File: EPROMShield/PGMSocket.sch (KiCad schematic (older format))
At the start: 22 parts

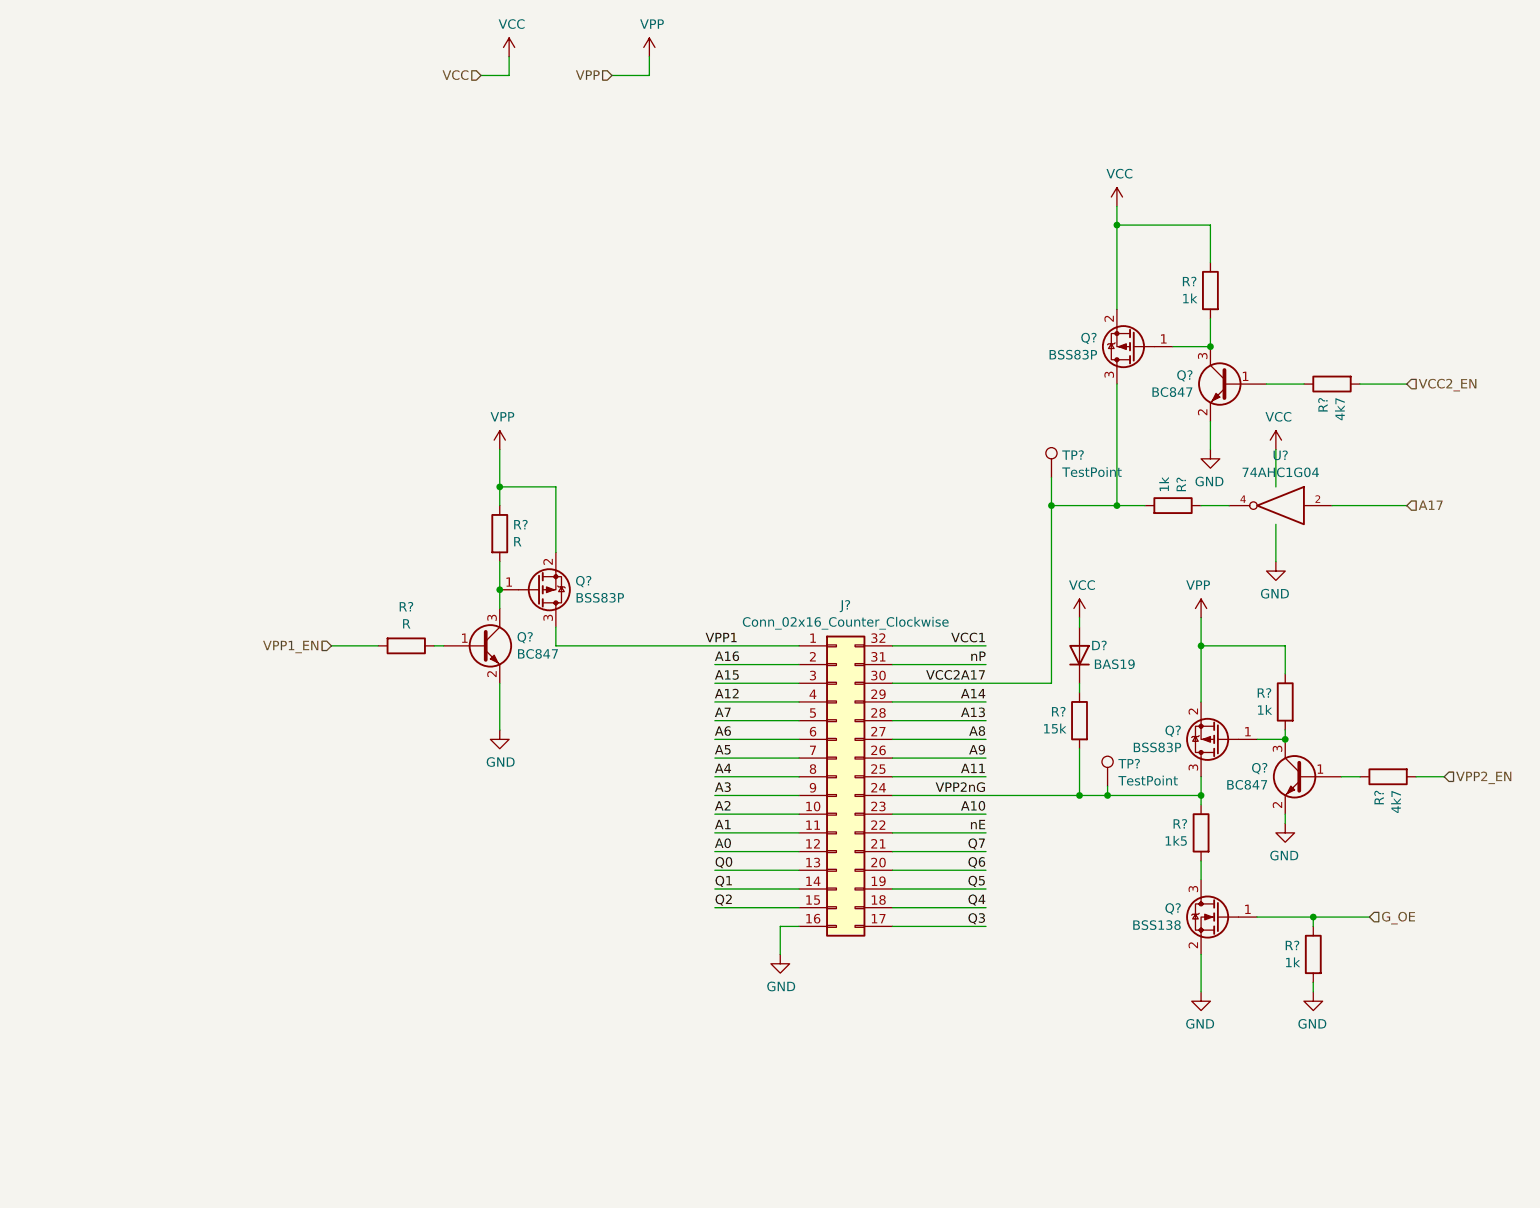
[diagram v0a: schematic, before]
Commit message: Finished schematic added caluclation for boost converter
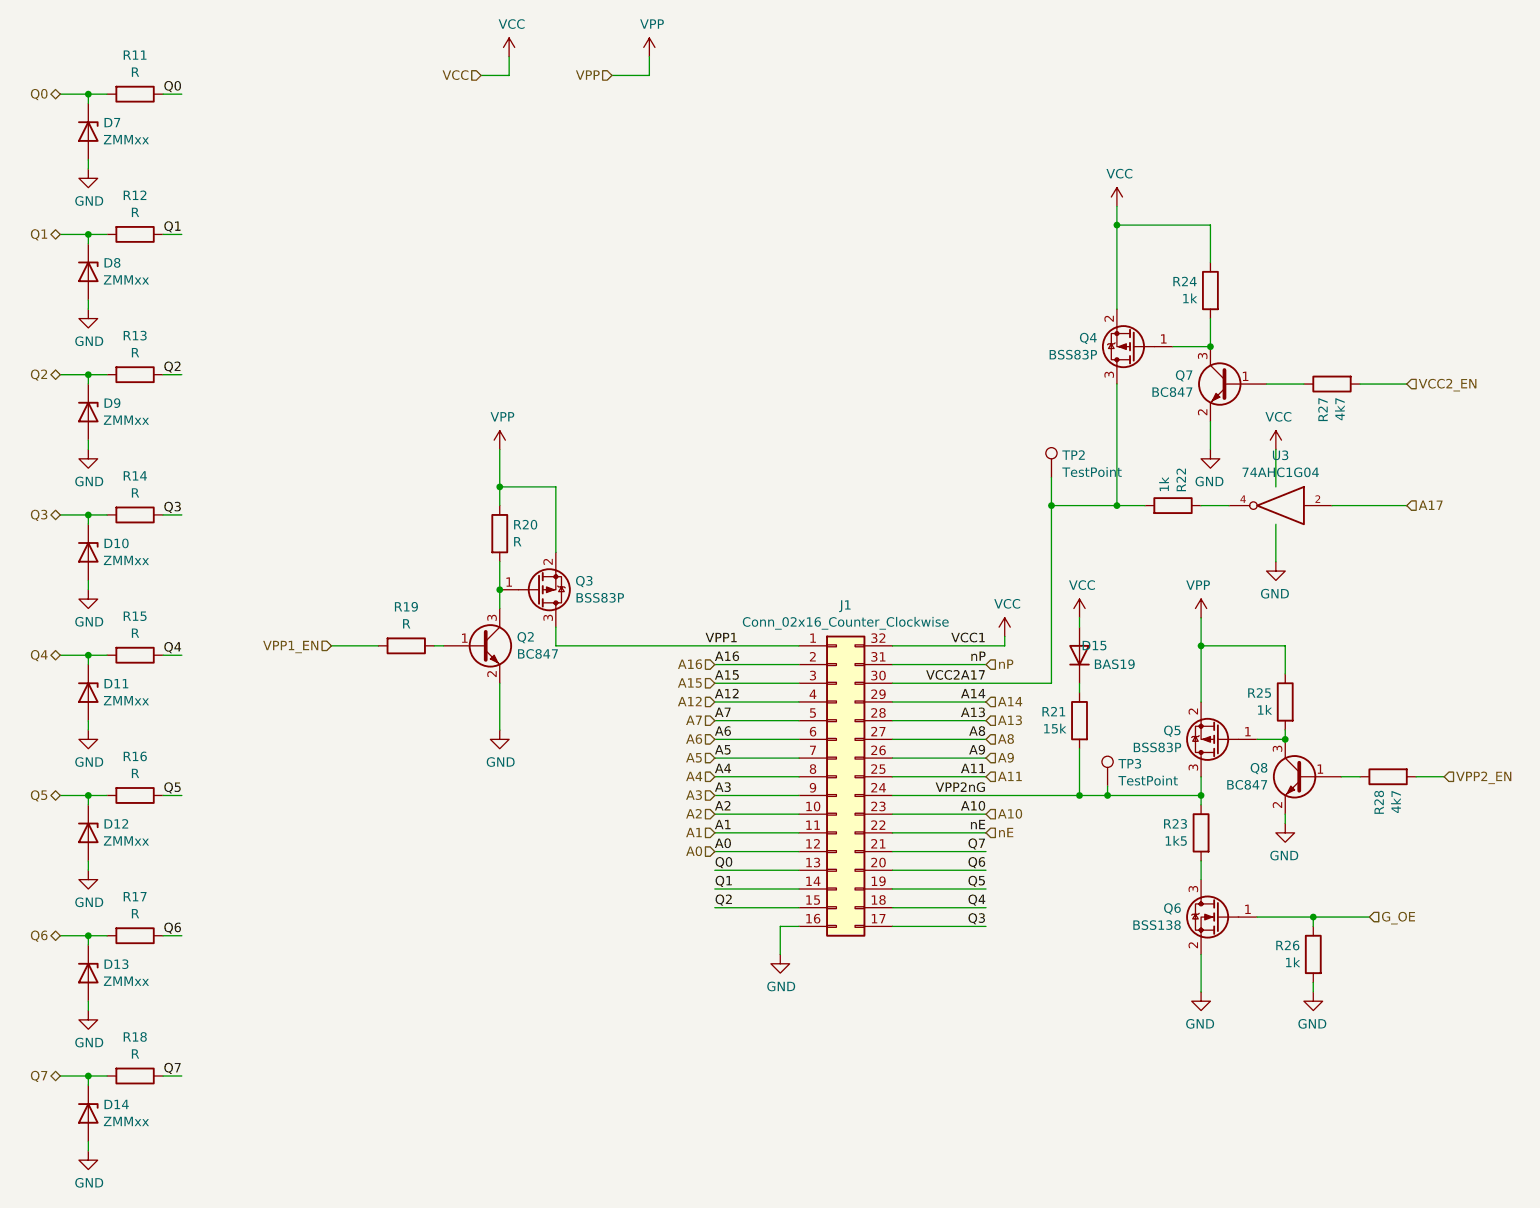
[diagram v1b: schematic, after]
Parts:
- added D10, D11, D12, D13, D14, D7, D8, D9: ZMMxx, Diode_SMD:D_MiniMELF, symbol Diode:ZMMxx
- added R11, R12, R13, R14, R15, R16, R17, R18: R, symbol Device:R
- gave numbers to parts that had none: 22
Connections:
- net VCC1 is gone; now on net VCC: J1.32 (Pin_32)
- net GND: now also D10.2 (A), D11.2 (A), D12.2 (A), D13.2 (A), D14.2 (A), D7.2 (A), D8.2 (A), D9.2 (A)
- net Q0: now also D7.1 (K), R11.1, R11.2
- net Q1: now also D8.1 (K), R12.1, R12.2
- net Q2: now also D9.1 (K), R13.1, R13.2
- net Q3: now also D10.1 (K), R14.1, R14.2
- net Q4: now also D11.1 (K), R15.1, R15.2
- net Q5: now also D12.1 (K), R16.1, R16.2
- net Q6: now also D13.1 (K), R17.1, R17.2
- net Q7: now also D14.1 (K), R18.1, R18.2

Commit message: Footprints associated
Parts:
- removed U3: 74AHC1G04, symbol 74xGxx:74AHC1G04
- added U3: 74AHC1GU04, Package_TO_SOT_SMD:SOT-353_SC-70-5_Handsoldering, symbol 74xGxx:74AHC1GU04
- J1: footprint (none) -> Socket:DIP_Socket-32_W11.9_W12.7_W15.24_W17.78_W18.5_3M_232-1285-00-0602J
- R11, R12, R13, R14, R15, R16, R17, R18: value R -> 1k2; footprint (none) -> Resistor_SMD:R_0805_2012Metric_Pad1.20x1.40mm_HandSolder
- R19: value R -> 4k7; footprint (none) -> Resistor_SMD:R_0805_2012Metric_Pad1.20x1.40mm_HandSolder
- R20: value R -> 10k; footprint (none) -> Resistor_SMD:R_0805_2012Metric_Pad1.20x1.40mm_HandSolder
- R21, R22, R23, R26, R27, R28: footprint (none) -> Resistor_SMD:R_0805_2012Metric_Pad1.20x1.40mm_HandSolder
- R24, R25: value 1k -> 10k; footprint (none) -> Resistor_SMD:R_0805_2012Metric_Pad1.20x1.40mm_HandSolder
- TP2, TP3: footprint (none) -> TestPoint:TestPoint_Pad_D2.0mm
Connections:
- net VCC is gone; now on net GND: D15.1 (A), J1.32 (Pin_32), Q4.2 (S), R24.1
- net A17: now also U3.2
- net GND: now also U3.3 (GND), U3.5 (VCC)
- net at R22.1: now also U3.4
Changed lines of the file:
@@
 F 0 "J1" H 5300 5517 50  0000 C CNN
 F 1 "Conn_02x16_Counter_Clockwise" H 5300 5426 50  0000 C CNN
-F 2 "" H 5250 4600 50  0001 C CNN
+F 2 "Socket:DIP_Socket-32_W11.9_W12.7_W15.24_W17.78_W18.5_3M_232-1285-00-0602J" H 5250 4600 50  0001 C CNN
 F 3 "~" H 5250 4600 50  0001 C CNN
 	1    5250 4600
@@
 P 3450 3300
 F 0 "R20" H 3520 3346 50  0000 L CNN
-F 1 "R" H 3520 3255 50  0000 L CNN
-F 2 "" V 3380 3300 50  0001 C CNN
+F 1 "10k" H 3520 3255 50  0000 L CNN
+F 2 "Resistor_SMD:R_0805_2012Metric_Pad1.20x1.40mm_HandSolder" V 3380 3300 50  0001 C CNN
 F 3 "~" H 3450 3300 50  0001 C CNN
 	1    3450 3300
@@
 AR Path="/6126FB03/616FB69F" Ref="R19"  Part="1"
 F 0 "R19" V 2743 3900 50  0000 C CNN
-F 1 "R" V 2834 3900 50  0000 C CNN
-F 2 "" V 2880 3900 50  0001 C CNN
+F 1 "4k7" V 2834 3900 50  0000 C CNN
+F 2 "Resistor_SMD:R_0805_2012Metric_Pad1.20x1.40mm_HandSolder" V 2880 3900 50  0001 C CNN
 F 3 "~" H 2950 3900 50  0001 C CNN
 	1    2950 3900
@@
 P 7650 4200
 F 0 "R25" H 7720 4246 50  0000 L CNN
-F 1 "1k" H 7720 4155 50  0000 L CNN
-F 2 "" V 7580 4200 50  0001 C CNN
+F 1 "10k" H 7720 4155 50  0000 L CNN
+F 2 "Resistor_SMD:R_0805_2012Metric_Pad1.20x1.40mm_HandSolder" V 7580 4200 50  0001 C CNN
 F 3 "~" H 7650 4200 50  0001 C CNN
 	1    7650 4200
@@
 F 0 "R28" H 8270 4646 50  0000 L CNN
 F 1 "4k7" H 8270 4555 50  0000 L CNN
-F 2 "" V 8130 4600 50  0001 C CNN
+F 2 "Resistor_SMD:R_0805_2012Metric_Pad1.20x1.40mm_HandSolder" V 8130 4600 50  0001 C CNN
 F 3 "~" H 8200 4600 50  0001 C CNN
 	1    8200 4600
@@
 F 0 "R26" H 7870 5596 50  0000 L CNN
 F 1 "1k" H 7870 5505 50  0000 L CNN
-F 2 "" V 7730 5550 50  0001 C CNN
+F 2 "Resistor_SMD:R_0805_2012Metric_Pad1.20x1.40mm_HandSolder" V 7730 5550 50  0001 C CNN
 F 3 "~" H 7800 5550 50  0001 C CNN
 	1    7800 5550
@@
 F 0 "R23" H 7270 4946 50  0000 L CNN
 F 1 "1k5" H 7270 4855 50  0000 L CNN
-F 2 "" V 7130 4900 50  0001 C CNN
+F 2 "Resistor_SMD:R_0805_2012Metric_Pad1.20x1.40mm_HandSolder" V 7130 4900 50  0001 C CNN
 F 3 "~" H 7200 4900 50  0001 C CNN
 	1    7200 4900
@@
 Wire Wire Line
 	7200 5050 7200 5150
-$Comp
-L 74xGxx:74AHC1G04 U3
-U 1 1 616FB717
-P 7600 3150
-F 0 "U3" H 7575 3417 50  0000 C CNN
-F 1 "74AHC1G04" H 7575 3326 50  0000 C CNN
-F 2 "" H 7600 3150 50  0001 C CNN
-F 3 "http://www.ti.com/lit/sg/scyt129e/scyt129e.pdf" H 7600 3150 50  0001 C CNN
-	1    7600 3150
-	-1   0    0    -1
-$EndComp
 $Comp
 L power:VCC #PWR?
@@
 F 0 "R27" H 7970 2546 50  0000 L CNN
 F 1 "4k7" H 7970 2455 50  0000 L CNN
-F 2 "" V 7830 2500 50  0001 C CNN
+F 2 "Resistor_SMD:R_0805_2012Metric_Pad1.20x1.40mm_HandSolder" V 7830 2500 50  0001 C CNN
 F 3 "~" H 7900 2500 50  0001 C CNN
 	1    7900 2500
@@
 P 7250 2000
 F 0 "R24" H 7320 2046 50  0000 L CNN
-F 1 "1k" H 7320 1955 50  0000 L CNN
-F 2 "" V 7180 2000 50  0001 C CNN
+F 1 "10k" H 7320 1955 50  0000 L CNN
+F 2 "Resistor_SMD:R_0805_2012Metric_Pad1.20x1.40mm_HandSolder" V 7180 2000 50  0001 C CNN
 F 3 "~" H 7250 2000 50  0001 C CNN
 	1    7250 2000
@@
 F 0 "R22" H 7120 3196 50  0000 L CNN
 F 1 "1k" H 7120 3105 50  0000 L CNN
-F 2 "" V 6980 3150 50  0001 C CNN
+F 2 "Resistor_SMD:R_0805_2012Metric_Pad1.20x1.40mm_HandSolder" V 6980 3150 50  0001 C CNN
 F 3 "~" H 7050 3150 50  0001 C CNN
 	1    7050 3150
@@
 F 0 "R21" H 6620 4346 50  0000 L CNN
 F 1 "15k" H 6620 4255 50  0000 L CNN
-F 2 "" V 6480 4300 50  0001 C CNN
+F 2 "Resistor_SMD:R_0805_2012Metric_Pad1.20x1.40mm_HandSolder" V 6480 4300 50  0001 C CNN
 F 3 "~" H 6550 4300 50  0001 C CNN
 	1    6550 4300
@@
 F 0 "TP3" H 6758 4768 50  0000 L CNN
 F 1 "TestPoint" H 6758 4677 50  0000 L CNN
-F 2 "" H 6900 4650 50  0001 C CNN
+F 2 "TestPoint:TestPoint_Pad_D2.0mm" H 6900 4650 50  0001 C CNN
 F 3 "~" H 6900 4650 50  0001 C CNN
 	1    6700 4650
@@
 F 0 "TP2" H 6458 3118 50  0000 L CNN
 F 1 "TestPoint" H 6458 3027 50  0000 L CNN
-F 2 "" H 6600 3000 50  0001 C CNN
+F 2 "TestPoint:TestPoint_Pad_D2.0mm" H 6600 3000 50  0001 C CNN
 F 3 "~" H 6600 3000 50  0001 C CNN
 	1    6400 3000
@@
 P 1500 950
 F 0 "R11" V 1293 950 50  0000 C CNN
-F 1 "R" V 1384 950 50  0000 C CNN
-F 2 "" V 1430 950 50  0001 C CNN
+F 1 "1k2" V 1384 950 50  0000 C CNN
+F 2 "Resistor_SMD:R_0805_2012Metric_Pad1.20x1.40mm_HandSolder" V 1430 950 50  0001 C CNN
 F 3 "~" H 1500 950 50  0001 C CNN
 	1    1500 950
@@
 P 1500 1700
 F 0 "R12" V 1293 1700 50  0000 C CNN
-F 1 "R" V 1384 1700 50  0000 C CNN
-F 2 "" V 1430 1700 50  0001 C CNN
+F 1 "1k2" V 1384 1700 50  0000 C CNN
+F 2 "Resistor_SMD:R_0805_2012Metric_Pad1.20x1.40mm_HandSolder" V 1430 1700 50  0001 C CNN
 F 3 "~" H 1500 1700 50  0001 C CNN
 	1    1500 1700
@@
 P 1500 2450
 F 0 "R13" V 1293 2450 50  0000 C CNN
-F 1 "R" V 1384 2450 50  0000 C CNN
-F 2 "" V 1430 2450 50  0001 C CNN
+F 1 "1k2" V 1384 2450 50  0000 C CNN
+F 2 "Resistor_SMD:R_0805_2012Metric_Pad1.20x1.40mm_HandSolder" V 1430 2450 50  0001 C CNN
 F 3 "~" H 1500 2450 50  0001 C CNN
 	1    1500 2450
@@
 P 1500 3200
 F 0 "R14" V 1293 3200 50  0000 C CNN
-F 1 "R" V 1384 3200 50  0000 C CNN
-F 2 "" V 1430 3200 50  0001 C CNN
+F 1 "1k2" V 1384 3200 50  0000 C CNN
+F 2 "Resistor_SMD:R_0805_2012Metric_Pad1.20x1.40mm_HandSolder" V 1430 3200 50  0001 C CNN
 F 3 "~" H 1500 3200 50  0001 C CNN
 	1    1500 3200
@@
 P 1500 3950
 F 0 "R15" V 1293 3950 50  0000 C CNN
-F 1 "R" V 1384 3950 50  0000 C CNN
-F 2 "" V 1430 3950 50  0001 C CNN
+F 1 "1k2" V 1384 3950 50  0000 C CNN
+F 2 "Resistor_SMD:R_0805_2012Metric_Pad1.20x1.40mm_HandSolder" V 1430 3950 50  0001 C CNN
 F 3 "~" H 1500 3950 50  0001 C CNN
 	1    1500 3950
@@
 P 1500 4700
 F 0 "R16" V 1293 4700 50  0000 C CNN
-F 1 "R" V 1384 4700 50  0000 C CNN
-F 2 "" V 1430 4700 50  0001 C CNN
+F 1 "1k2" V 1384 4700 50  0000 C CNN
+F 2 "Resistor_SMD:R_0805_2012Metric_Pad1.20x1.40mm_HandSolder" V 1430 4700 50  0001 C CNN
 F 3 "~" H 1500 4700 50  0001 C CNN
 	1    1500 4700
@@
 P 1500 5450
 F 0 "R17" V 1293 5450 50  0000 C CNN
-F 1 "R" V 1384 5450 50  0000 C CNN
-F 2 "" V 1430 5450 50  0001 C CNN
+F 1 "1k2" V 1384 5450 50  0000 C CNN
+F 2 "Resistor_SMD:R_0805_2012Metric_Pad1.20x1.40mm_HandSolder" V 1430 5450 50  0001 C CNN
 F 3 "~" H 1500 5450 50  0001 C CNN
 	1    1500 5450
@@
 P 1500 6200
 F 0 "R18" V 1293 6200 50  0000 C CNN
-F 1 "R" V 1384 6200 50  0000 C CNN
-F 2 "" V 1430 6200 50  0001 C CNN
+F 1 "1k2" V 1384 6200 50  0000 C CNN
+F 2 "Resistor_SMD:R_0805_2012Metric_Pad1.20x1.40mm_HandSolder" V 1430 6200 50  0001 C CNN
 F 3 "~" H 1500 6200 50  0001 C CNN
 	1    1500 6200
@@
 Text Label 1750 6200 2    50   ~ 0
 Q7
+$Comp
+L 74xGxx:74AHC1GU04 U3
+U 1 1 615B34B7
+P 7600 3150
+F 0 "U3" H 7575 2883 50  0000 C CNN
+F 1 "74AHC1GU04" H 7575 2974 50  0000 C CNN
+F 2 "Package_TO_SOT_SMD:SOT-353_SC-70-5_Handsoldering" H 7600 3150 50  0001 C CNN
+F 3 "http://www.ti.com/lit/sg/scyt129e/scyt129e.pdf" H 7600 3150 50  0001 C CNN
+	1    7600 3150
+	-1   0    0    1
+$EndComp
 $EndSCHEMATC

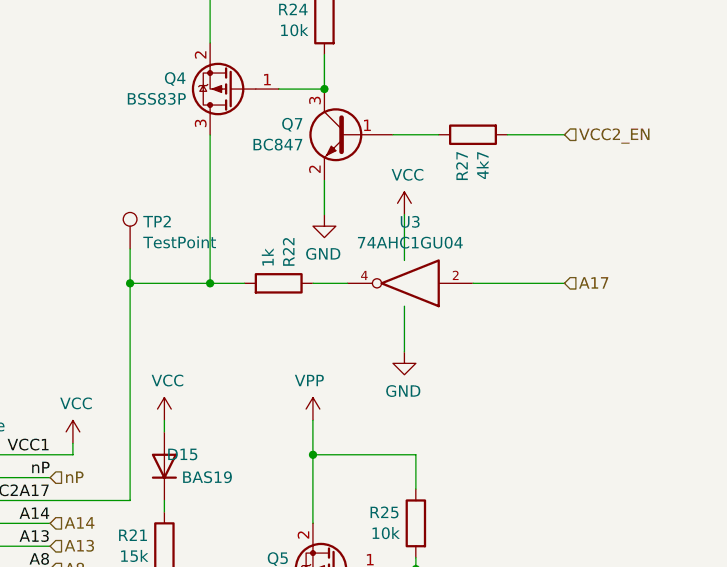
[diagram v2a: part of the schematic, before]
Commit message: First shot at component placement. Fixed VCC connection for Inverter
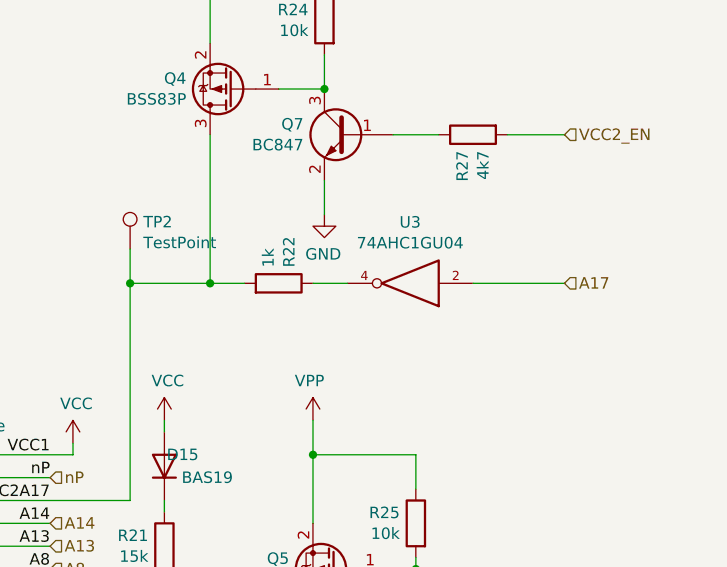
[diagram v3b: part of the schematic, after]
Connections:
- net GND: no longer D15.1 (A), J1.32 (Pin_32), Q4.2 (S), R24.1, U3.5 (VCC)
- new net VCC: D15.1 (A), J1.32 (Pin_32), Q4.2 (S), R24.1, U3.5 (VCC)
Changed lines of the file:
@@
 	7900 3150 8300 3150
-$Comp
-L power:VCC #PWR0137
-U 1 1 616FB765
-P 7600 2850
-F 0 "#PWR0137" H 7600 2700 50  0001 C CNN
-F 1 "VCC" H 7615 3023 50  0000 C CNN
-F 2 "" H 7600 2850 50  0001 C CNN
-F 3 "" H 7600 2850 50  0001 C CNN
-	1    7600 2850
-	1    0    0    -1
-$EndComp
-Wire Wire Line
-	7600 2850 7600 3050
-Wire Wire Line
-	7600 3250 7600 3450
-$Comp
-L power:GND #PWR0138
-U 1 1 616FB76D
-P 7600 3450
-F 0 "#PWR0138" H 7600 3200 50  0001 C CNN
-F 1 "GND" H 7605 3277 50  0000 C CNN
-F 2 "" H 7600 3450 50  0001 C CNN
-F 3 "" H 7600 3450 50  0001 C CNN
-	1    7600 3450
-	-1   0    0    -1
-$EndComp
 $Comp
 L Connector:TestPoint TP3

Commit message: First Version routing is done
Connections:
- net Q0: no longer D7.1 (K), R11.2
- net Q1: no longer D8.1 (K), R12.2
- net Q2: no longer D9.1 (K), R13.2
- net Q3: no longer D10.1 (K), R14.2
- net Q4: no longer D11.1 (K), R15.2
- net Q5: no longer D12.1 (K), R16.2
- net Q6: no longer D13.1 (K), R17.2
- net Q7: no longer D14.1 (K), R18.2
- new net PQ0: D7.1 (K), R11.2
- new net PQ1: D8.1 (K), R12.2
- new net PQ2: D9.1 (K), R13.2
- new net PQ3: D10.1 (K), R14.2
- new net PQ4: D11.1 (K), R15.2
- new net PQ5: D12.1 (K), R16.2
- new net PQ6: D13.1 (K), R17.2
- new net PQ7: D14.1 (K), R18.2
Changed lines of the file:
@@
 Text Label 4600 4700 0    50   ~ 0
 A3
-Text Label 4600 4600 0    50   ~ 0
-A4
-Text Label 4600 4500 0    50   ~ 0
-A5
 Text Label 4600 4400 0    50   ~ 0
 A6
@@
 Text HLabel 4600 4400 0    50   Input ~ 0
 A6
-Text HLabel 4600 4500 0    50   Input ~ 0
-A5
-Text HLabel 4600 4600 0    50   Input ~ 0
-A4
 Text HLabel 4600 4700 0    50   Input ~ 0
 A3
@@
 	1250 950  1100 950
 Connection ~ 1250 950
-$Comp
-L power:GND #PWR0142
-U 1 1 612429D9
-P 1250 1350
-F 0 "#PWR0142" H 1250 1100 50  0001 C CNN
-F 1 "GND" H 1255 1177 50  0000 C CNN
-F 2 "" H 1250 1350 50  0001 C CNN
-F 3 "" H 1250 1350 50  0001 C CNN
-	1    1250 1350
-	1    0    0    -1
-$EndComp
 Wire Wire Line
 	1250 1300 1250 1350
@@
 	1650 950  1750 950
 Text HLabel 1100 950  0    50   BiDi ~ 0
-Q0
+PQ0
 $Comp
 L Diode:ZMMxx D8
@@
 	1650 1700 1750 1700
 Text HLabel 1100 1700 0    50   BiDi ~ 0
-Q1
+PQ1
 $Comp
 L Diode:ZMMxx D9
@@
 	1650 2450 1750 2450
 Text HLabel 1100 2450 0    50   BiDi ~ 0
-Q2
+PQ2
 $Comp
 L Diode:ZMMxx D10
@@
 	1650 3200 1750 3200
 Text HLabel 1100 3200 0    50   BiDi ~ 0
-Q3
+PQ3
 $Comp
 L Diode:ZMMxx D11
@@
 	1650 3950 1750 3950
 Text HLabel 1100 3950 0    50   BiDi ~ 0
-Q4
+PQ4
 $Comp
 L Diode:ZMMxx D12
@@
 	1650 4700 1750 4700
 Text HLabel 1100 4700 0    50   BiDi ~ 0
-Q5
+PQ5
 $Comp
 L Diode:ZMMxx D13
@@
 	1650 5450 1750 5450
 Text HLabel 1100 5450 0    50   BiDi ~ 0
-Q6
+PQ6
 $Comp
 L Diode:ZMMxx D14
@@
 	1650 6200 1750 6200
 Text HLabel 1100 6200 0    50   BiDi ~ 0
-Q7
+PQ7
 Text Label 1750 950  2    50   ~ 0
 Q0
@@
 	-1   0    0    1
 $EndComp
+$Comp
+L power:GND #PWR?
+U 1 1 6128EAC7
+P 1250 1350
+F 0 "#PWR?" H 1250 1100 50  0001 C CNN
+F 1 "GND" H 1255 1177 50  0000 C CNN
+F 2 "" H 1250 1350 50  0001 C CNN
+F 3 "" H 1250 1350 50  0001 C CNN
+	1    1250 1350
+	1    0    0    -1
+$EndComp
+Text HLabel 4600 4600 0    50   Input ~ 0
+A4
+Text HLabel 4600 4500 0    50   Input ~ 0
+A5
+Text Label 4600 4600 0    50   ~ 0
+A4
+Text Label 4600 4500 0    50   ~ 0
+A5
 $EndSCHEMATC
